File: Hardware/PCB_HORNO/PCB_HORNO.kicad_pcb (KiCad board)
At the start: 2 copper layers, 226.2 x 263.7 mm, 254 parts, among them J0_1 Screw_Terminal_01x03, J0_10 Screw_Terminal_01x03, J0_13 Screw_Terminal_01x03, J0_14 Screw_Terminal_01x03, J0_16 Screw_Terminal_01x03, J0_18 Screw_Terminal_01x03, J0_19 Screw_Terminal_01x03, J0_2 Screw_Terminal_01x03, J0_20 Screw_Terminal_01x03, J0_21 Screw_Terminal_01x03, J0_22 Screw_Terminal_01x03, J0_23 Screw_Terminal_01x03, J0_24 Screw_Terminal_01x03, J0_25 Screw_Terminal_01x03, J0_26 Screw_Terminal_01x03, J0_3 Screw_Terminal_01x03, J0_5 Screw_Terminal_01x03, J0_6 Screw_Terminal_01x03, J0_7 Screw_Terminal_01x03, J0_8 Screw_Terminal_01x03, J0_9 Screw_Terminal_01x03, J1 Screw_Terminal_01x20, J2 Screw_Terminal_01x20, J3 Screw_Terminal_01x20, J4 Screw_Terminal_01x20, K1 Fujitsu_FTR-LYCA005x, K2 Fujitsu_FTR-LYCA005x, K3 Fujitsu_FTR-LYCA005x, K4 Fujitsu_FTR-LYCA005x, Q1 2N2222, Q2 2N2222, Q3 2N2222, Q4 2N2222, Q5 BTA16-800B, Q6 IRG4PF50W, Q7 IRG4PF50W, U1 TLP521-1, U10 LM741, U11 LM741, U12 LM741, U13 MOC3021M, U14 TLP521-1, U15 TLP250, U16 TLP521-1, U17 LM741, U18 LM741, U19 TLP250, U2 TLP521-1, U20 L298HN, U21 TLP521-1, U22 TLP521-1, U23 TLP521-1, U3 TLP521-1, U4 TLP521-1, U5 TLP521-1, U6 TLP521-1, U7 TLP521-1, U8 TLP521-1, U9 LM741

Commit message: Ajuste de pads
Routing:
- net Net-(J0_21-Pin_2): track 14.7 -> 24.1 mm, vias 0 -> 1
- net Net-(J0_5-Pin_2): track 72.6 -> 80.1 mm
- net Net-(J0_5-Pin_3): track 57.0 -> 62.3 mm
- net Net-(GND1-Pin_1): track 1214.3 -> 1218.3 mm
- net Net-(D13-A): track 56.9 -> 53.0 mm
- net Net-(D9-A): track 50.9 -> 54.8 mm
- net Net-(3V3a1-Pin_1): track 212.1 -> 215.4 mm
- net Net-(J0_5-Pin_1): track 87.7 -> 90.9 mm
- net Net-(J0_6-Pin_1): track 37.2 -> 33.9 mm
- net Net-(R48-Pad1): track 15.2 -> 12.7 mm
- net Net-(3V3b1-Pin_1): track 98.5 -> 100.8 mm
- net Net-(PS7--Vout): track 148.1 -> 150.4 mm
- net Net-(R46-Pad1): track 11.3 -> 9.00 mm
- net Net-(PS6-+Vout): track 217.9 -> 219.5 mm
- net Net-(D12-A): track 53.5 -> 51.8 mm
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
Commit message: Corrección de ruteo
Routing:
- net Net-(PS6-+Vout): track 219.5 -> 163.8 mm
- net Net-(J1-Pin_5): track 12.3 -> 67.0 mm, vias 0 -> 1
- net Net-(J0_9-Pin_1): track 68.7 -> 40.1 mm
- net Net-(J0_16-Pin_2): track 48.0 -> 67.4 mm, vias 1 -> 0
- net Net-(J0_1-Pin_1): track 150.0 -> 131.8 mm
- net Net-(J0_10-Pin_3): track 26.6 -> 44.7 mm, vias 0 -> 1
- net Net-(D9-A): track 54.8 -> 39.8 mm
- net Net-(PX124-Pin_1): track 15.3 -> 29.9 mm
- net Net-(D13-A): track 53.0 -> 39.8 mm
- net Net-(U20-SENSE_B): track 48.8 -> 35.9 mm, vias 0 -> 2
- net Net-(D12-A): track 51.8 -> 39.8 mm
- net Net-(R49-Pad2): track 104.8 -> 115.8 mm
- net Net-(PS2--Vout): track 24.6 -> 34.4 mm
- net Net-(3V3a1-Pin_1): track 215.4 -> 225.0 mm, vias 1 -> 2
- net Net-(J0_21-Pin_2): track 24.1 -> 14.7 mm, vias 1 -> 0
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
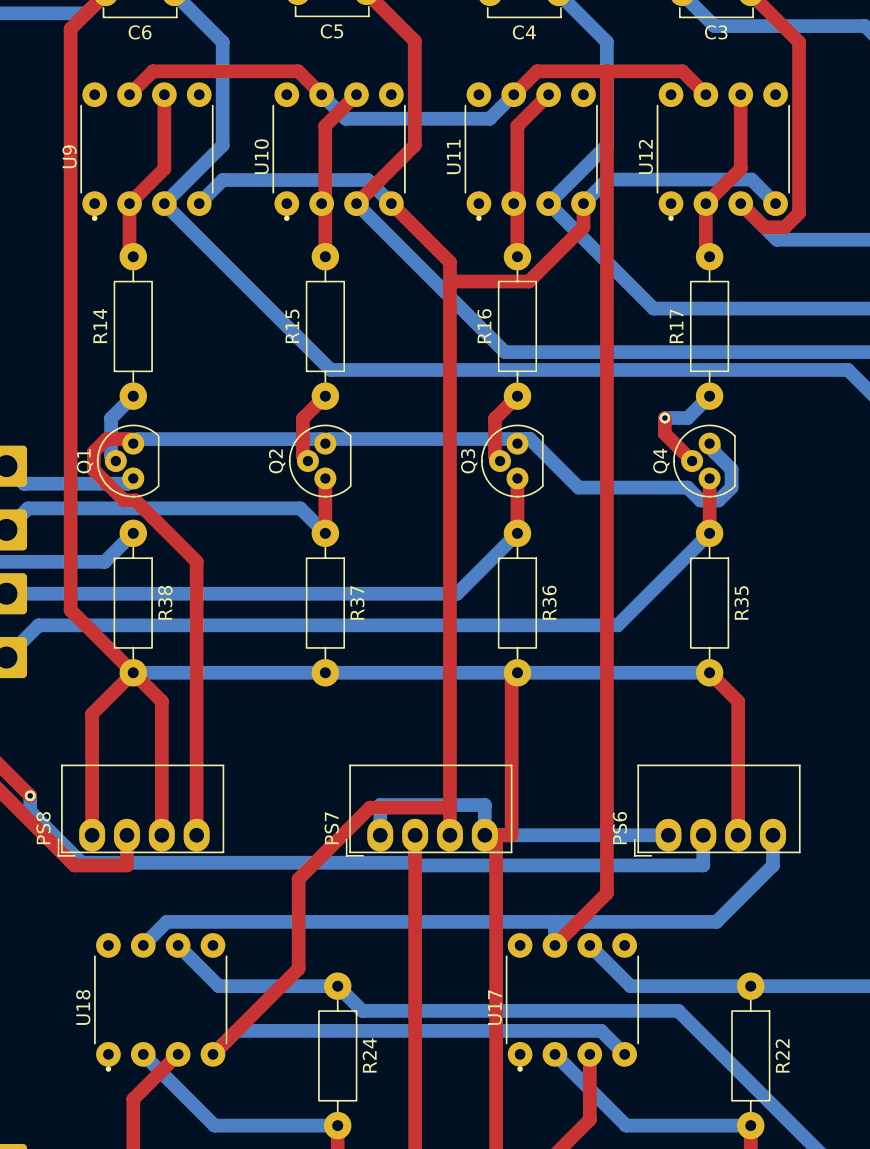
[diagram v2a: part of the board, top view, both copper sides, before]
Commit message: Ajustes a las interfaces digital y analogica
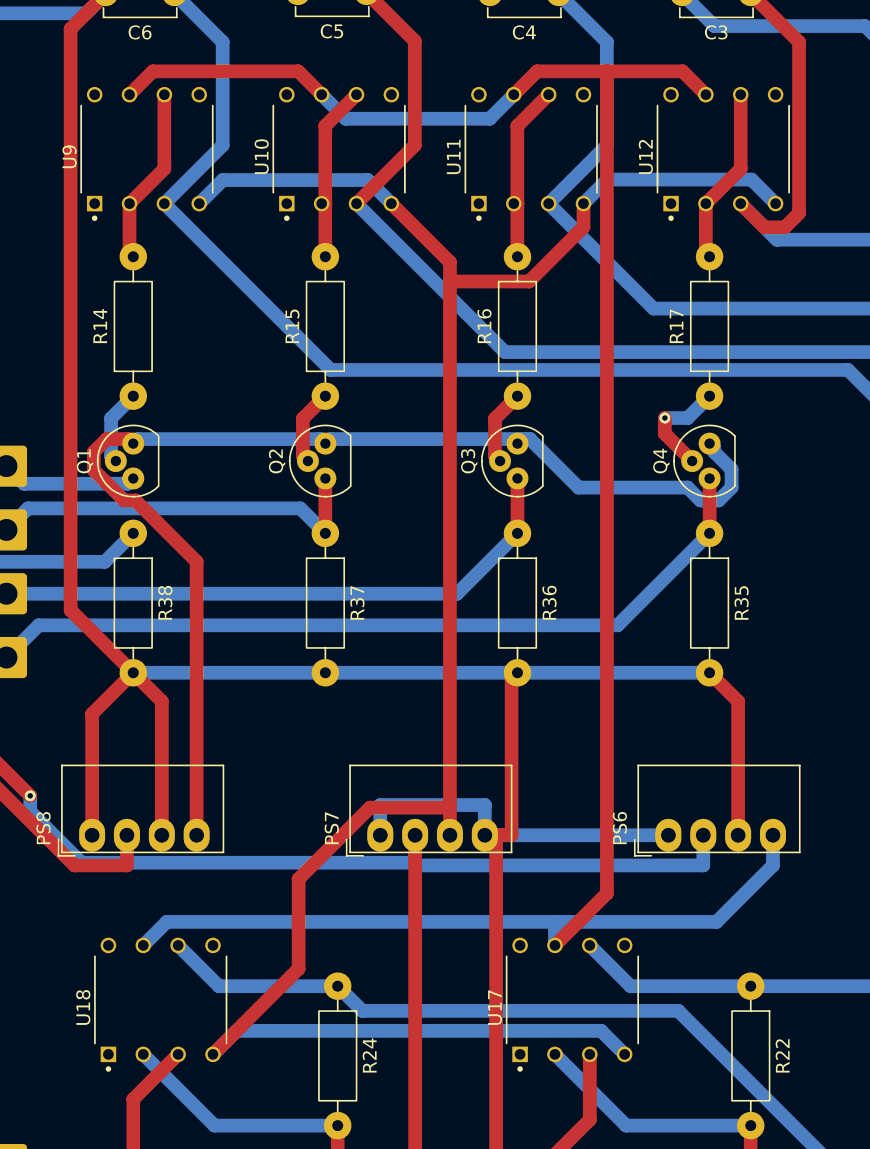
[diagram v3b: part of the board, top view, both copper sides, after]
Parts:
- U10, U11, U12, U17, U18, U9: footprint LM741_TH:LM471_TH -> LM741_TH:LM741_TH
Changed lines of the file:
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@@
 		)
 	)
-	(footprint "LM741_TH:LM471_TH"
+	(footprint "LM741_TH:LM741_TH"
 		(layer "F.Cu")
 		(at 233 34 90)
@@
 		)
 		(property "Value" "LM741"
-			(at 0.1525 5.6 90)
+			(at 10.865 5.607 90)
 			(layer "F.Fab")
 			(effects
@@
 			(layer "F.Fab")
 		)
-		(pad "1" thru_hole circle
+		(pad "1" thru_hole rect
 			(at -3.97 -3.81 90)
-			(size 1.8 1.8)
+			(size 1.13 1.13)
 			(drill 0.78)
 			(layers "*.Cu" "*.Mask")
@@
 		(pad "2" thru_hole circle
 			(at -3.97 -1.27 90)
-			(size 1.8 1.8)
+			(size 1.13 1.13)
 			(drill 0.78)
 			(layers "*.Cu" "*.Mask")
@@
 		(pad "3" thru_hole circle
 			(at -3.97 1.27 90)
-			(size 1.8 1.8)
+			(size 1.13 1.13)
 			(drill 0.78)
 			(layers "*.Cu" "*.Mask")
@@
 		(pad "4" thru_hole circle
 			(at -3.97 3.81 90)
-			(size 1.8 1.8)
+			(size 1.13 1.13)
 			(drill 0.78)
 			(layers "*.Cu" "*.Mask")
@@
 		(pad "5" thru_hole circle
 			(at 3.97 3.81 90)
-			(size 1.8 1.8)
+			(size 1.13 1.13)
 			(drill 0.78)
 			(layers "*.Cu" "*.Mask")
@@
 		(pad "6" thru_hole circle
 			(at 3.97 1.27 90)
-			(size 1.8 1.8)
+			(size 1.13 1.13)
 			(drill 0.78)
 			(layers "*.Cu" "*.Mask")
@@
 		(pad "7" thru_hole circle
 			(at 3.97 -1.27 90)
-			(size 1.8 1.8)
+			(size 1.13 1.13)
 			(drill 0.78)
 			(layers "*.Cu" "*.Mask")
@@
 		(pad "8" thru_hole circle
 			(at 3.97 -3.81 90)
-			(size 1.8 1.8)
+			(size 1.13 1.13)
 			(drill 0.78)
 			(layers "*.Cu" "*.Mask")
@@
 		)
 		(embedded_fonts no)
-		(model "C:/Users/Bojtronic/Documents/KiCad/9.0/library/LM741/LM741CN_NOPB.step"
+		(model "/home/bojorge/Documents/TEC/TFG/Kicad library/LM741CN_NOPB/LM741CN_NOPB.step"
 			(offset
 				(xyz 0 0 0)
@@
 		)
 	)
-	(footprint "LM741_TH:LM471_TH"
+	(footprint "LM741_TH:LM741_TH"
 		(layer "F.Cu")
 		(at 219 34 90)
@@
 		)
 		(property "Value" "LM741"
-			(at 0.1525 5.6 90)
+			(at 10.865 5.607 90)
 			(layer "F.Fab")
 			(effects
@@
 			(layer "F.Fab")
 		)
-		(pad "1" thru_hole circle
+		(pad "1" thru_hole rect
 			(at -3.97 -3.81 90)
-			(size 1.8 1.8)
+			(size 1.13 1.13)
 			(drill 0.78)
 			(layers "*.Cu" "*.Mask")
@@
 		(pad "2" thru_hole circle
 			(at -3.97 -1.27 90)
-			(size 1.8 1.8)
+			(size 1.13 1.13)
 			(drill 0.78)
 			(layers "*.Cu" "*.Mask")
@@
 		(pad "3" thru_hole circle
 			(at -3.97 1.27 90)
-			(size 1.8 1.8)
+			(size 1.13 1.13)
 			(drill 0.78)
 			(layers "*.Cu" "*.Mask")
@@
 		(pad "4" thru_hole circle
 			(at -3.97 3.81 90)
-			(size 1.8 1.8)
+			(size 1.13 1.13)
 			(drill 0.78)
 			(layers "*.Cu" "*.Mask")
@@
 		(pad "5" thru_hole circle
 			(at 3.97 3.81 90)
-			(size 1.8 1.8)
+			(size 1.13 1.13)
 			(drill 0.78)
 			(layers "*.Cu" "*.Mask")
@@
 		(pad "6" thru_hole circle
 			(at 3.97 1.27 90)
-			(size 1.8 1.8)
+			(size 1.13 1.13)
 			(drill 0.78)
 			(layers "*.Cu" "*.Mask")
@@
 		(pad "7" thru_hole circle
 			(at 3.97 -1.27 90)
-			(size 1.8 1.8)
+			(size 1.13 1.13)
 			(drill 0.78)
 			(layers "*.Cu" "*.Mask")
@@
 		(pad "8" thru_hole circle
 			(at 3.97 -3.81 90)
-			(size 1.8 1.8)
+			(size 1.13 1.13)
 			(drill 0.78)
 			(layers "*.Cu" "*.Mask")
@@
 		)
 		(embedded_fonts no)
-		(model "C:/Users/Bojtronic/Documents/KiCad/9.0/library/LM741/LM741CN_NOPB.step"
+		(model "/home/bojorge/Documents/TEC/TFG/Kicad library/LM741CN_NOPB/LM741CN_NOPB.step"
 			(offset
 				(xyz 0 0 0)
@@
 		)
 	)
-	(footprint "LM741_TH:LM471_TH"
+	(footprint "LM741_TH:LM741_TH"
 		(layer "F.Cu")
 		(at 190.9975 34 90)
@@
 		)
 		(property "Value" "LM741"
-			(at 0.1525 5.6 90)
+			(at 10.865 5.607 90)
 			(layer "F.Fab")
 			(effects
@@
 			(layer "F.Fab")
 		)
-		(pad "1" thru_hole circle
+		(pad "1" thru_hole rect
 			(at -3.97 -3.81 90)
-			(size 1.8 1.8)
+			(size 1.13 1.13)
 			(drill 0.78)
 			(layers "*.Cu" "*.Mask")
@@
 		(pad "2" thru_hole circle
 			(at -3.97 -1.27 90)
-			(size 1.8 1.8)
+			(size 1.13 1.13)
 			(drill 0.78)
 			(layers "*.Cu" "*.Mask")
@@
 		(pad "3" thru_hole circle
 			(at -3.97 1.27 90)
-			(size 1.8 1.8)
+			(size 1.13 1.13)
 			(drill 0.78)
 			(layers "*.Cu" "*.Mask")
@@
 		(pad "4" thru_hole circle
 			(at -3.97 3.81 90)
-			(size 1.8 1.8)
+			(size 1.13 1.13)
 			(drill 0.78)
 			(layers "*.Cu" "*.Mask")
@@
 		(pad "5" thru_hole circle
 			(at 3.97 3.81 90)
-			(size 1.8 1.8)
+			(size 1.13 1.13)
 			(drill 0.78)
 			(layers "*.Cu" "*.Mask")
@@
 		(pad "6" thru_hole circle
 			(at 3.97 1.27 90)
-			(size 1.8 1.8)
+			(size 1.13 1.13)
 			(drill 0.78)
 			(layers "*.Cu" "*.Mask")
@@
 		(pad "7" thru_hole circle
 			(at 3.97 -1.27 90)
-			(size 1.8 1.8)
+			(size 1.13 1.13)
 			(drill 0.78)
 			(layers "*.Cu" "*.Mask")
@@
 		(pad "8" thru_hole circle
 			(at 3.97 -3.81 90)
-			(size 1.8 1.8)
+			(size 1.13 1.13)
 			(drill 0.78)
 			(layers "*.Cu" "*.Mask")
@@
 		)
 		(embedded_fonts no)
-		(model "C:/Users/Bojtronic/Documents/KiCad/9.0/library/LM741/LM741CN_NOPB.step"
+		(model "/home/bojorge/Documents/TEC/TFG/Kicad library/LM741CN_NOPB/LM741CN_NOPB.step"
 			(offset
 				(xyz 0 0 0)
@@
 		)
 	)
-	(footprint "LM741_TH:LM471_TH"
+	(footprint "LM741_TH:LM741_TH"
 		(layer "F.Cu")
 		(at 192 96 90)
@@
 		)
 		(property "Value" "LM741"
-			(at 0.1875 5.5 90)
+			(at 10.865 5.607 90)
 			(layer "F.Fab")
 			(effects
@@
 			(layer "F.Fab")
 		)
-		(pad "1" thru_hole circle
+		(pad "1" thru_hole rect
 			(at -3.97 -3.81 90)
-			(size 1.8 1.8)
+			(size 1.13 1.13)
 			(drill 0.78)
 			(layers "*.Cu" "*.Mask")
@@
 		(pad "2" thru_hole circle
 			(at -3.97 -1.27 90)
-			(size 1.8 1.8)
+			(size 1.13 1.13)
 			(drill 0.78)
 			(layers "*.Cu" "*.Mask")
@@
 		(pad "3" thru_hole circle
 			(at -3.97 1.27 90)
-			(size 1.8 1.8)
+			(size 1.13 1.13)
 			(drill 0.78)
 			(layers "*.Cu" "*.Mask")
@@
 		(pad "4" thru_hole circle
 			(at -3.97 3.81 90)
-			(size 1.8 1.8)
+			(size 1.13 1.13)
 			(drill 0.78)
 			(layers "*.Cu" "*.Mask")
@@
 		(pad "5" thru_hole circle
 			(at 3.97 3.81 90)
-			(size 1.8 1.8)
+			(size 1.13 1.13)
 			(drill 0.78)
 			(layers "*.Cu" "*.Mask")
@@
 		(pad "6" thru_hole circle
 			(at 3.97 1.27 90)
-			(size 1.8 1.8)
+			(size 1.13 1.13)
 			(drill 0.78)
 			(layers "*.Cu" "*.Mask")
@@
 		(pad "7" thru_hole circle
 			(at 3.97 -1.27 90)
-			(size 1.8 1.8)
+			(size 1.13 1.13)
 			(drill 0.78)
 			(layers "*.Cu" "*.Mask")
@@
 		(pad "8" thru_hole circle
 			(at 3.97 -3.81 90)
-			(size 1.8 1.8)
+			(size 1.13 1.13)
 			(drill 0.78)
 			(layers "*.Cu" "*.Mask")
@@
 		)
 		(embedded_fonts no)
-		(model "C:/Users/Bojtronic/Documents/KiCad/9.0/library/LM741/LM741CN_NOPB.step"
+		(model "/home/bojorge/Documents/TEC/TFG/Kicad library/LM741CN_NOPB/LM741CN_NOPB.step"
 			(offset
 				(xyz 0 0 0)
@@
 		)
 	)
-	(footprint "LM741_TH:LM471_TH"
+	(footprint "LM741_TH:LM741_TH"
 		(layer "F.Cu")
 		(at 222 96 90)
@@
 		)
 		(property "Value" "LM741"
-			(at 0.1875 5.5 90)
+			(at 10.865 5.607 90)
 			(layer "F.Fab")
 			(effects
@@
 			(layer "F.Fab")
 		)
-		(pad "1" thru_hole circle
+		(pad "1" thru_hole rect
 			(at -3.97 -3.81 90)
-			(size 1.8 1.8)
+			(size 1.13 1.13)
 			(drill 0.78)
 			(layers "*.Cu" "*.Mask")
@@
 		(pad "2" thru_hole circle
 			(at -3.97 -1.27 90)
-			(size 1.8 1.8)
+			(size 1.13 1.13)
 			(drill 0.78)
 			(layers "*.Cu" "*.Mask")
@@
 		(pad "3" thru_hole circle
 			(at -3.97 1.27 90)
-			(size 1.8 1.8)
+			(size 1.13 1.13)
 			(drill 0.78)
 			(layers "*.Cu" "*.Mask")
@@
 		(pad "4" thru_hole circle
 			(at -3.97 3.81 90)
-			(size 1.8 1.8)
+			(size 1.13 1.13)
 			(drill 0.78)
 			(layers "*.Cu" "*.Mask")
@@
 		(pad "5" thru_hole circle
 			(at 3.97 3.81 90)
-			(size 1.8 1.8)
+			(size 1.13 1.13)
 			(drill 0.78)
 			(layers "*.Cu" "*.Mask")
@@
 		(pad "6" thru_hole circle
 			(at 3.97 1.27 90)
-			(size 1.8 1.8)
+			(size 1.13 1.13)
 			(drill 0.78)
 			(layers "*.Cu" "*.Mask")
@@
 		(pad "7" thru_hole circle
 			(at 3.97 -1.27 90)
-			(size 1.8 1.8)
+			(size 1.13 1.13)
 			(drill 0.78)
 			(layers "*.Cu" "*.Mask")
@@
 		(pad "8" thru_hole circle
 			(at 3.97 -3.81 90)
-			(size 1.8 1.8)
+			(size 1.13 1.13)
 			(drill 0.78)
 			(layers "*.Cu" "*.Mask")
@@
 		)
 		(embedded_fonts no)
-		(model "C:/Users/Bojtronic/Documents/KiCad/9.0/library/LM741/LM741CN_NOPB.step"
+		(model "/home/bojorge/Documents/TEC/TFG/Kicad library/LM741CN_NOPB/LM741CN_NOPB.step"
 			(offset
 				(xyz 0 0 0)
@@
 		)
 	)
-	(footprint "LM741_TH:LM471_TH"
+	(footprint "LM741_TH:LM741_TH"
 		(layer "F.Cu")
 		(at 205 34 90)
@@
 		)
 		(property "Value" "LM741"
-			(at 0.1525 5.6 90)
+			(at 10.865 5.607 90)
 			(layer "F.Fab")
 			(effects
@@
 			(layer "F.Fab")
 		)
-		(pad "1" thru_hole circle
+		(pad "1" thru_hole rect
 			(at -3.97 -3.81 90)
-			(size 1.8 1.8)
+			(size 1.13 1.13)
 			(drill 0.78)
 			(layers "*.Cu" "*.Mask")
@@
 		(pad "2" thru_hole circle
 			(at -3.97 -1.27 90)
-			(size 1.8 1.8)
+			(size 1.13 1.13)
 			(drill 0.78)
 			(layers "*.Cu" "*.Mask")
@@
 		(pad "3" thru_hole circle
 			(at -3.97 1.27 90)
-			(size 1.8 1.8)
+			(size 1.13 1.13)
 			(drill 0.78)
 			(layers "*.Cu" "*.Mask")
@@
 		(pad "4" thru_hole circle
 			(at -3.97 3.81 90)
-			(size 1.8 1.8)
+			(size 1.13 1.13)
 			(drill 0.78)
 			(layers "*.Cu" "*.Mask")
@@
 		(pad "5" thru_hole circle
 			(at 3.97 3.81 90)
-			(size 1.8 1.8)
+			(size 1.13 1.13)
 			(drill 0.78)
 			(layers "*.Cu" "*.Mask")
@@
 		(pad "6" thru_hole circle
 			(at 3.97 1.27 90)
-			(size 1.8 1.8)
+			(size 1.13 1.13)
 			(drill 0.78)
 			(layers "*.Cu" "*.Mask")
@@
 		(pad "7" thru_hole circle
 			(at 3.97 -1.27 90)
-			(size 1.8 1.8)
+			(size 1.13 1.13)
 			(drill 0.78)
 			(layers "*.Cu" "*.Mask")
@@
 		(pad "8" thru_hole circle
 			(at 3.97 -3.81 90)
-			(size 1.8 1.8)
+			(size 1.13 1.13)
 			(drill 0.78)
 			(layers "*.Cu" "*.Mask")
@@
 		)
 		(embedded_fonts no)
-		(model "C:/Users/Bojtronic/Documents/KiCad/9.0/library/LM741/LM741CN_NOPB.step"
+		(model "/home/bojorge/Documents/TEC/TFG/Kicad library/LM741CN_NOPB/LM741CN_NOPB.step"
 			(offset
 				(xyz 0 0 0)
